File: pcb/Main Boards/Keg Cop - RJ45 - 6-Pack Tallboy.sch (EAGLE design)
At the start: 6 parts, among them X2 RJ45-8X

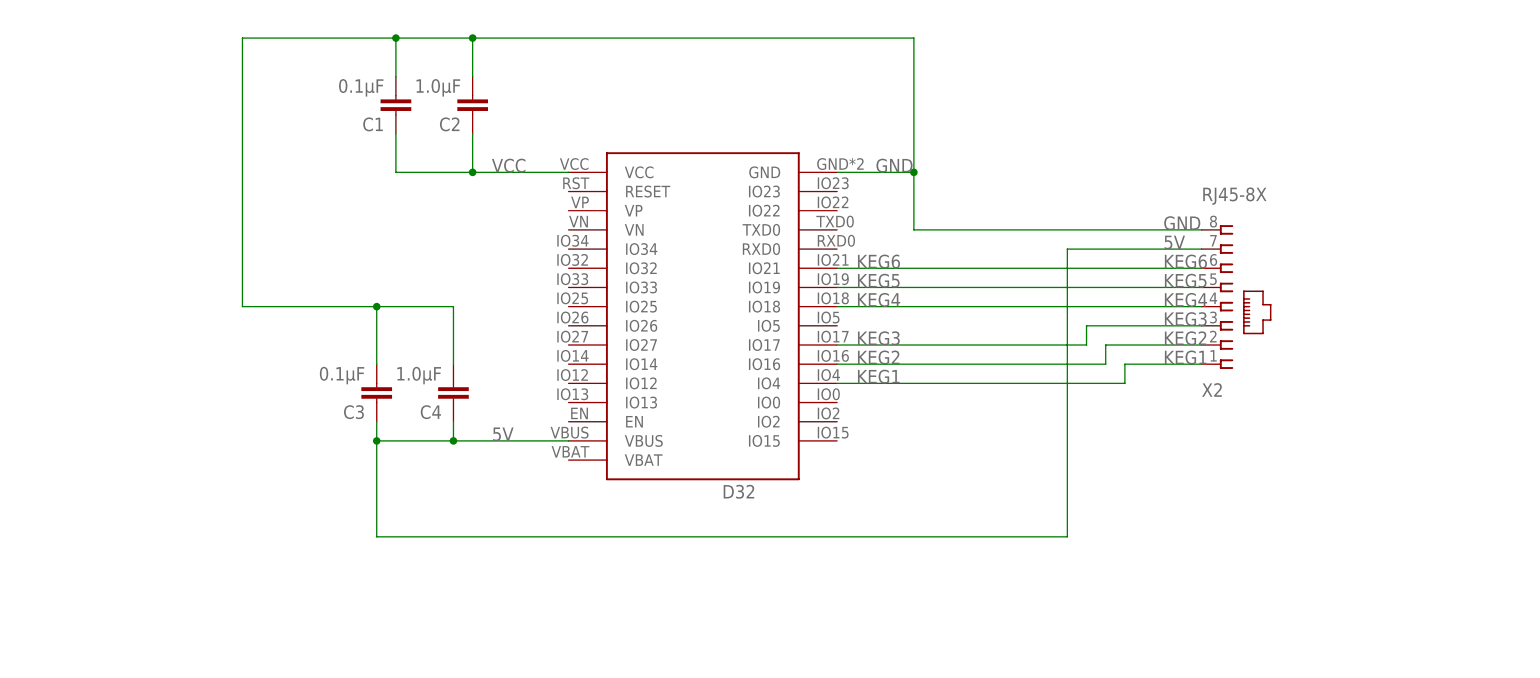
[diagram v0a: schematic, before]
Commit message: Swap pins, split dirs
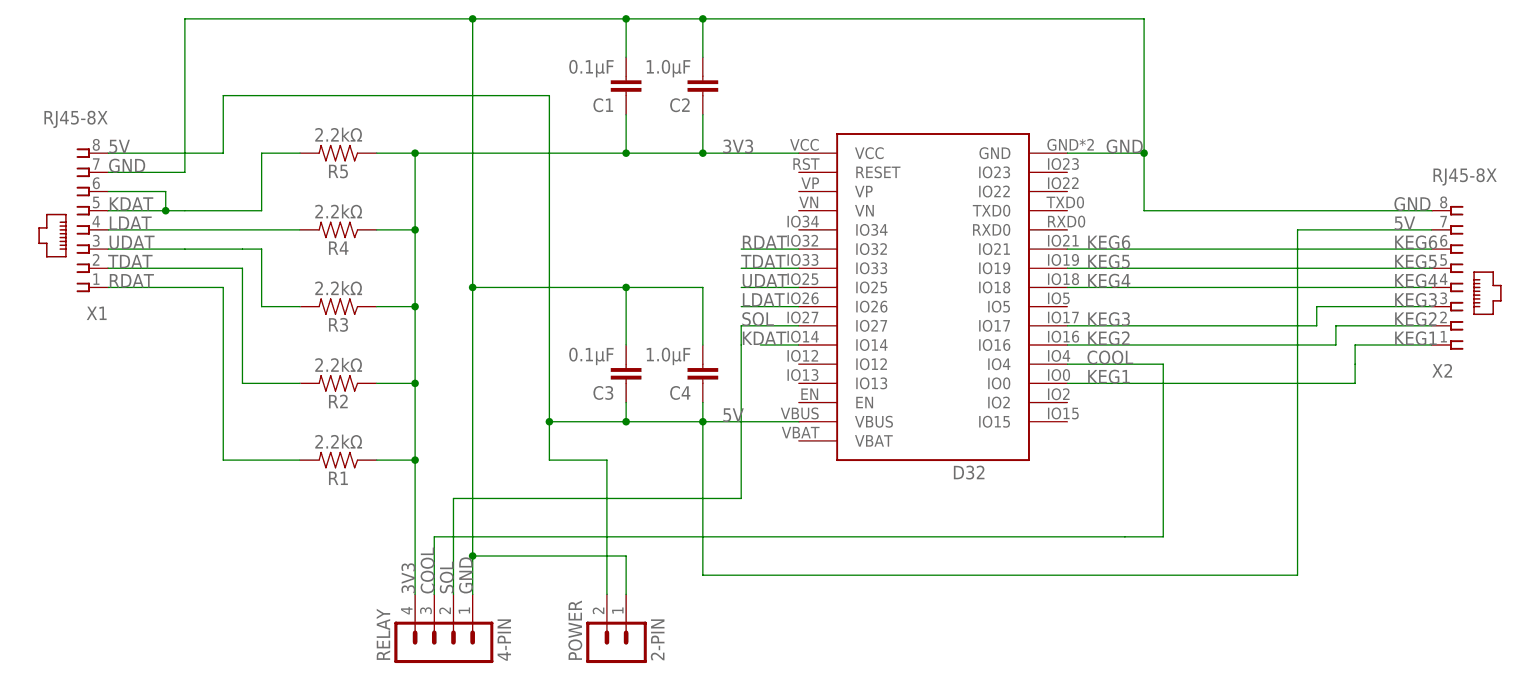
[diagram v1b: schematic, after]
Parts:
- added POWER: 2-PIN, Donnie:HDR-2
- added R1, R2, R3, R4, R5: 2.2kΩ, SparkFun-Resistors:RESISTORAXIAL-0.3
- added RELAY: 4-PIN, Donnie:MA04-1
- added X1: RJ45-8X, con-tycoelectronics:RJ45-8X
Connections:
- removed net VCC: C1.1, C2.1, D32.VCC
- new net 3V3: C1.1, C2.1, D32.VCC, R1.1, R2.1, R3.1, R4.1, R5.1, RELAY.4
- new net COOL: D32.IO4, RELAY.3
- new net KDAT: D32.IO14, R5.2, X1.5, X1.6
- new net LDAT: D32.IO26, R4.2, X1.4
- new net RDAT: D32.IO32, R1.2, X1.1
- new net SOL: D32.IO27, RELAY.2
- new net TDAT: D32.IO33, R2.2, X1.2
- new net UDAT: D32.IO25, R3.2, X1.3
- net 5V: now also POWER.2, X1.8
- net GND: now also POWER.1, RELAY.1, X1.7
- net KEG1: now also D32.IO0; no longer D32.IO4
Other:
- moved on the sheet: C1, C2, C3, C4, D32, X2

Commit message: Renamed files
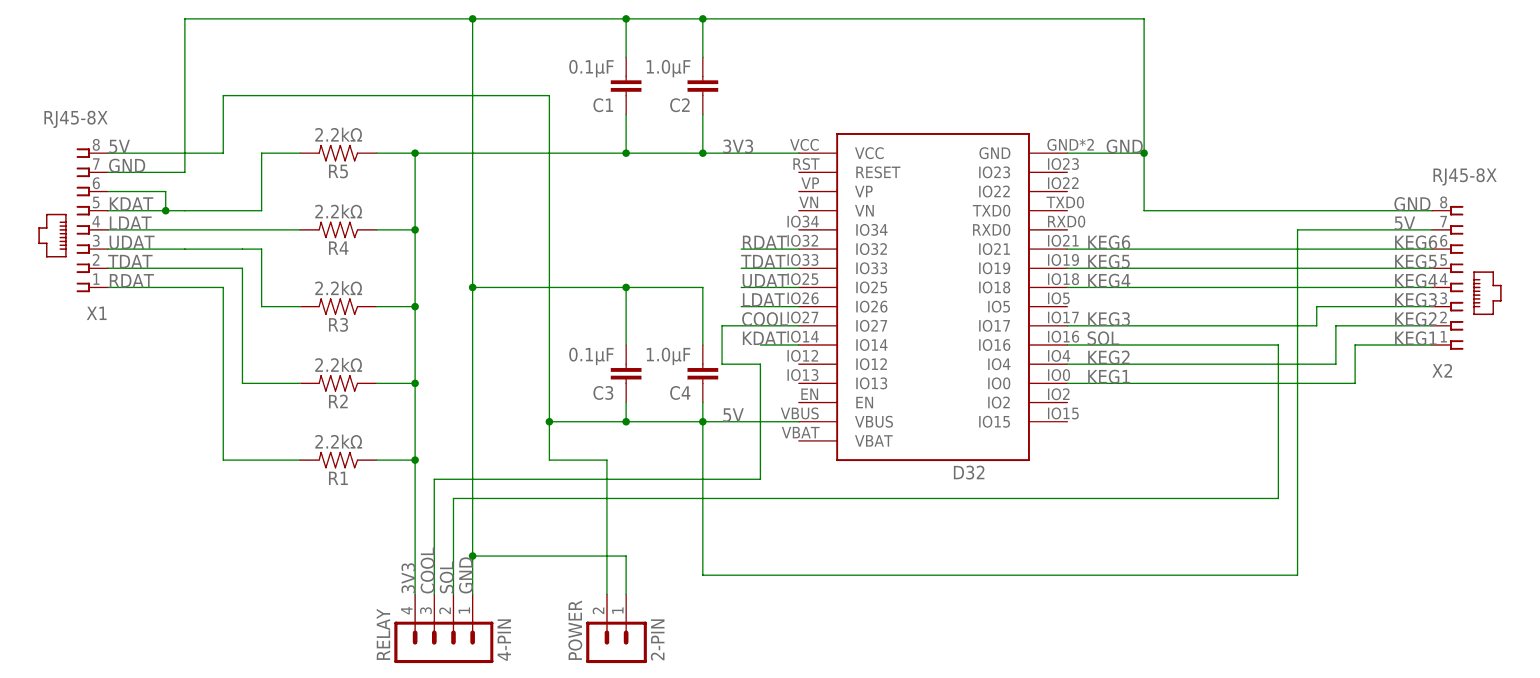
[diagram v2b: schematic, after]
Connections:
- net COOL: now also D32.IO27; no longer D32.IO4
- net KEG2: now also D32.IO4; no longer D32.IO16
- net SOL: now also D32.IO16; no longer D32.IO27
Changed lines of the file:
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@@
-</segment>
-</net>
-<net name="SOL" class="0">
-<segment>
-<wire x1="20.32" y1="45.72" x2="20.32" y2="25.4" width="0.1524" layer="91"/>
-<wire x1="20.32" y1="25.4" x2="-17.78" y2="25.4" width="0.1524" layer="91"/>
-<pinref part="RELAY" gate="1" pin="2"/>
-<wire x1="-17.78" y1="25.4" x2="-17.78" y2="12.7" width="0.1524" layer="91"/>
-<label x="-17.78" y="12.7" size="1.778" layer="95" rot="R90"/>
-<wire x1="20.32" y1="45.72" x2="20.32" y2="48.26" width="0.1524" layer="91"/>
-<pinref part="D32" gate="G$1" pin="IO27"/>
-<wire x1="20.32" y1="48.26" x2="27.94" y2="48.26" width="0.1524" layer="91"/>
-<label x="20.32" y="48.26" size="1.778" layer="95"/>
-</segment>
-</net>
-<net name="COOL" class="0">
-<segment>
-<wire x1="71.12" y1="20.32" x2="-20.32" y2="20.32" width="0.1524" layer="91"/>
-<pinref part="RELAY" gate="1" pin="3"/>
-<wire x1="-20.32" y1="20.32" x2="-20.32" y2="12.7" width="0.1524" layer="91"/>
-<label x="-20.32" y="12.7" size="1.778" layer="95" rot="R90"/>
-<wire x1="71.12" y1="20.32" x2="76.2" y2="20.32" width="0.1524" layer="91"/>
-<wire x1="76.2" y1="20.32" x2="76.2" y2="43.18" width="0.1524" layer="91"/>
-<pinref part="D32" gate="G$1" pin="IO4"/>
-<wire x1="76.2" y1="43.18" x2="63.5" y2="43.18" width="0.1524" layer="91"/>
-<label x="66.04" y="43.18" size="1.778" layer="95"/>
 </segment>
 </net>
@@
 <net name="KEG1" class="0">
 <segment>
-<wire x1="101.6" y1="43.18" x2="101.6" y2="45.72" width="0.1524" layer="91"/>
 <wire x1="101.6" y1="45.72" x2="111.76" y2="45.72" width="0.1524" layer="91"/>
 <label x="106.68" y="45.72" size="1.778" layer="95"/>
 <pinref part="X2" gate="G$1" pin="1"/>
+<wire x1="101.6" y1="45.72" x2="101.6" y2="40.64" width="0.1524" layer="91"/>
 <pinref part="D32" gate="G$1" pin="IO0"/>
-<wire x1="63.5" y1="40.64" x2="101.6" y2="40.64" width="0.1524" layer="91"/>
-<wire x1="101.6" y1="40.64" x2="101.6" y2="43.18" width="0.1524" layer="91"/>
+<wire x1="101.6" y1="40.64" x2="63.5" y2="40.64" width="0.1524" layer="91"/>
 <label x="66.04" y="40.64" size="1.778" layer="95"/>
 </segment>
@@
 <net name="KEG2" class="0">
 <segment>
-<pinref part="D32" gate="G$1" pin="IO16"/>
-<label x="66.04" y="45.72" size="1.778" layer="95"/>
-<wire x1="63.5" y1="45.72" x2="99.06" y2="45.72" width="0.1524" layer="91"/>
 <label x="106.68" y="48.26" size="1.778" layer="95"/>
 <pinref part="X2" gate="G$1" pin="2"/>
-<wire x1="99.06" y1="45.72" x2="99.06" y2="48.26" width="0.1524" layer="91"/>
 <wire x1="99.06" y1="48.26" x2="111.76" y2="48.26" width="0.1524" layer="91"/>
+<pinref part="D32" gate="G$1" pin="IO4"/>
+<wire x1="63.5" y1="43.18" x2="99.06" y2="43.18" width="0.1524" layer="91"/>
+<wire x1="99.06" y1="43.18" x2="99.06" y2="48.26" width="0.1524" layer="91"/>
+<label x="66.04" y="43.18" size="1.778" layer="95"/>
 </segment>
 </net>
@@
 </segment>
 </net>
+<net name="SOL" class="0">
+<segment>
+<pinref part="RELAY" gate="1" pin="2"/>
+<wire x1="-17.78" y1="12.7" x2="-17.78" y2="25.4" width="0.1524" layer="91"/>
+<wire x1="-17.78" y1="25.4" x2="91.44" y2="25.4" width="0.1524" layer="91"/>
+<wire x1="91.44" y1="25.4" x2="91.44" y2="45.72" width="0.1524" layer="91"/>
+<pinref part="D32" gate="G$1" pin="IO16"/>
+<wire x1="91.44" y1="45.72" x2="63.5" y2="45.72" width="0.1524" layer="91"/>
+<label x="-17.78" y="12.7" size="1.778" layer="95" rot="R90"/>
+<label x="66.04" y="45.72" size="1.778" layer="95"/>
+</segment>
+</net>
+<net name="COOL" class="0">
+<segment>
+<pinref part="RELAY" gate="1" pin="3"/>
+<wire x1="-20.32" y1="12.7" x2="-20.32" y2="27.94" width="0.1524" layer="91"/>
+<wire x1="-20.32" y1="27.94" x2="22.86" y2="27.94" width="0.1524" layer="91"/>
+<wire x1="22.86" y1="27.94" x2="22.86" y2="43.18" width="0.1524" layer="91"/>
+<wire x1="22.86" y1="43.18" x2="17.78" y2="43.18" width="0.1524" layer="91"/>
+<wire x1="17.78" y1="43.18" x2="17.78" y2="48.26" width="0.1524" layer="91"/>
+<pinref part="D32" gate="G$1" pin="IO27"/>
+<wire x1="17.78" y1="48.26" x2="27.94" y2="48.26" width="0.1524" layer="91"/>
+<label x="20.32" y="48.26" size="1.778" layer="95"/>
+<label x="-20.32" y="12.7" size="1.778" layer="95" rot="R90"/>
+</segment>
+</net>
